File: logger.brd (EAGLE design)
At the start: 99 x 44.1 mm, 77 parts, among them IC1 LTC4412, J1 POWER_JACKPTH, Q1 FDN360P, Q2 FDN360P, Q3 2N7002PW, Q4 2N7002PW, U1 DS3231MZ/V+T, U2 FT231X-Q

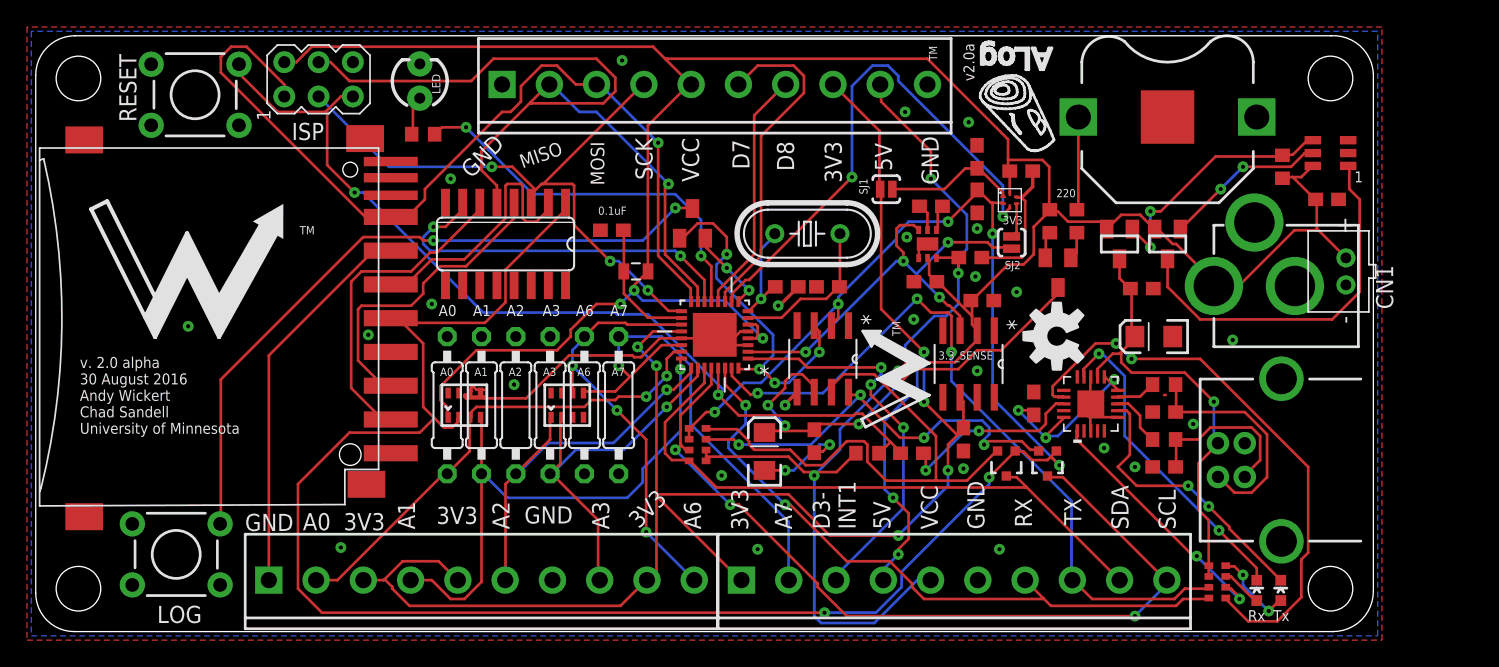
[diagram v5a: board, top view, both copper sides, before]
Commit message: Rerouted with VDD linked to RTC and SD; updated silk labels
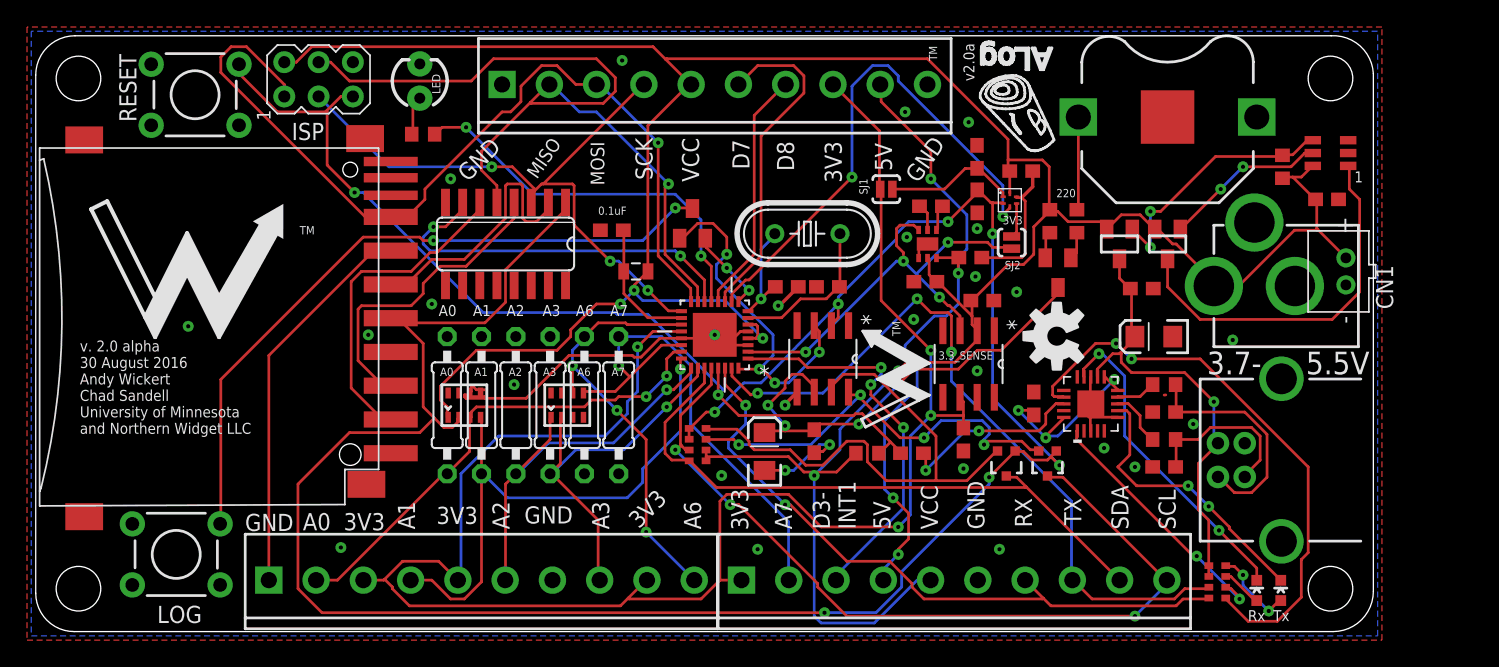
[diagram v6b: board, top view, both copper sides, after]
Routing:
- net +3V3: track 121.4 -> 131.3 mm, vias 6 -> 4
- net GND: vias 28 -> 29
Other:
- board text added: "3.7- 5.5V"
- board text added: "v. 2.0 alpha 30 August 2016 Andy Wickert Chad Sandell University of Minnesota and Northern Widget LLC"
- board text removed: "v. 2.0 alpha 30 August 2016 Andy Wickert Chad Sandell University of Minnesota"
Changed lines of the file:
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@@
 Andy Wickert
 Chad Sandell
-University of Minnesota</text>
+University of Minnesota
+and Northern Widget LLC</text>
 <text x="49.2787" y="7.5702" size="1.27" layer="21" rot="R90">A6</text>
 <text x="44.6686" y="7.5702" size="1.27" layer="21" rot="R45">3V3</text>
@@
 <text x="62.1481" y="36.1813" size="1.27" layer="21" rot="R270">5V</text>
 <text x="58.43" y="36.3083" size="1.27" layer="21" rot="R270">3V3</text>
-<text x="65.6025" y="36.6893" size="1.27" layer="21" rot="R270">GND</text>
+<text x="66.3645" y="36.8163" size="1.27" layer="21" rot="R235">GND</text>
 <text x="63.4365" y="22.987" size="0.6096" layer="21" rot="R270">TM</text>
 <text x="91.059" y="1.5875" size="0.8128" layer="21" rot="R180">Rx</text>
@@
 <text x="40.1076" y="18.9301" size="0.6096" layer="21">A6</text>
 <text x="42.6476" y="18.9301" size="0.6096" layer="21">A7</text>
-<text x="32.25503125" y="33.497734375" size="1.27" layer="21" rot="R45">GND</text>
-<text x="38.7802" y="36.3083" size="1.016" layer="21" rot="R199">MISO</text>
+<text x="32.00103125" y="33.243734375" size="1.27" layer="21" rot="R45">GND</text>
+<text x="38.1452" y="36.6893" size="1.016" layer="21" rot="R235">MISO</text>
 <text x="54.8965" y="36.3083" size="1.27" layer="21" rot="R270">D8</text>
 <text x="68.707" y="43.561" size="0.8128" layer="21" rot="R270">v2.0a</text>
+<text x="86.741" y="19.05" size="1.6764" layer="21">3.7-     5.5V</text>
 </plain>
 <attributes>
@@
 <contactref element="H1" pad="1"/>
 <contactref element="H0" pad="9"/>
-<wire x1="68.707" y1="17.018" x2="68.707" y2="15.074" width="0.2032" layer="1"/>
+<wire x1="68.707" y1="17.018" x2="68.707" y2="16.002" width="0.2032" layer="1"/>
+<wire x1="68.707" y1="16.002" x2="68.707" y2="15.074" width="0.2032" layer="1"/>
 <wire x1="68.453" y1="17.272" x2="68.707" y2="17.018" width="0.2032" layer="1"/>
 <wire x1="68.453" y1="17.272" x2="68.453" y2="17.3482" width="0.2032" layer="1"/>
@@
 <wire x1="31.242" y1="3.81" x2="29.845" y2="5.207" width="0.2032" layer="1"/>
 <wire x1="31.242" y1="3.81" x2="31.272" y2="3.81" width="0.2032" layer="1"/>
-<wire x1="45.72" y1="22.225" x2="47.8282" y2="22.225" width="0.2032" layer="1"/>
-<wire x1="44.577" y1="21.082" x2="45.72" y2="22.225" width="0.2032" layer="1"/>
-<wire x1="45.974" y1="19.685" x2="44.577" y2="21.082" width="0.2032" layer="16"/>
-<wire x1="45.974" y1="4.445" x2="45.974" y2="10.033" width="0.2032" layer="1"/>
-<wire x1="45.974" y1="10.033" x2="45.974" y2="10.16" width="0.2032" layer="1"/>
-<wire x1="45.974" y1="10.16" x2="45.974" y2="19.685" width="0.2032" layer="1"/>
-<wire x1="45.339" y1="3.81" x2="45.974" y2="4.445" width="0.2032" layer="1"/>
-<wire x1="45.339" y1="3.81" x2="45.272" y2="3.81" width="0.2032" layer="1"/>
-<wire x1="45.974" y1="10.033" x2="52.197" y2="3.81" width="0.2032" layer="1"/>
-<wire x1="52.197" y1="3.81" x2="52.272" y2="3.81" width="0.2032" layer="1"/>
 <wire x1="26.416" y1="3.302" x2="25.8445" y2="3.8735" width="0.2032" layer="1"/>
 <wire x1="26.416" y1="3.175" x2="26.416" y2="3.302" width="0.2032" layer="1"/>
 <wire x1="27.686" y1="1.905" x2="26.416" y2="3.175" width="0.2032" layer="1"/>
 <wire x1="43.307" y1="1.905" x2="27.686" y2="1.905" width="0.2032" layer="1"/>
-<wire x1="45.212" y1="3.81" x2="43.307" y2="1.905" width="0.2032" layer="1"/>
+<wire x1="45.212" y1="3.81" x2="43.8785" y2="2.4765" width="0.2032" layer="1"/>
+<wire x1="43.8785" y1="2.4765" x2="43.307" y2="1.905" width="0.2032" layer="1"/>
 <wire x1="45.212" y1="3.81" x2="45.272" y2="3.81" width="0.2032" layer="1"/>
-<wire x1="67.564" y1="13.843" x2="68.2625" y2="14.5415" width="0.2032" layer="1"/>
-<wire x1="68.2625" y1="14.5415" x2="68.707" y2="14.986" width="0.2032" layer="1"/>
-<wire x1="67.564" y1="11.938" x2="67.564" y2="13.843" width="0.2032" layer="1"/>
-<wire x1="67.564" y1="10.795" x2="67.564" y2="11.938" width="0.2032" layer="16"/>
-<wire x1="63.881" y1="7.112" x2="67.564" y2="10.795" width="0.2032" layer="16"/>
-<wire x1="58.801" y1="7.112" x2="63.881" y2="7.112" width="0.2032" layer="1"/>
-<wire x1="55.753" y1="10.16" x2="58.801" y2="7.112" width="0.2032" layer="1"/>
-<wire x1="45.974" y1="10.16" x2="55.753" y2="10.16" width="0.2032" layer="1"/>
-<wire x1="68.707" y1="14.986" x2="68.707" y2="15.074" width="0.2032" layer="1"/>
-<via x="44.577" y="21.082" extent="1-16" drill="0.3048"/>
-<via x="45.974" y="19.685" extent="1-16" drill="0.3048"/>
-<via x="67.564" y="11.938" extent="1-16" drill="0.3048"/>
-<via x="63.881" y="7.112" extent="1-16" drill="0.3048"/>
 <wire x1="62.484" y1="37.084" x2="62.484" y2="32.766" width="0.2032" layer="1"/>
 <wire x1="59.055" y1="40.513" x2="62.484" y2="37.084" width="0.2032" layer="1"/>
 <wire x1="62.484" y1="32.766" x2="62.544" y2="32.757" width="0.2032" layer="1"/>
 <wire x1="59.055" y1="40.513" x2="59.044" y2="40.513" width="0.2032" layer="1"/>
-<wire x1="62.611" y1="23.876" x2="62.611" y2="32.639" width="0.2032" layer="1"/>
-<wire x1="65.786" y1="20.701" x2="62.611" y2="23.876" width="0.2032" layer="1"/>
-<wire x1="65.786" y1="17.018" x2="65.786" y2="20.701" width="0.2032" layer="16"/>
-<wire x1="68.2625" y1="14.5415" x2="65.786" y2="17.018" width="0.2032" layer="1"/>
+<wire x1="66.294" y1="16.002" x2="68.707" y2="16.002" width="0.2032" layer="1"/>
+<wire x1="66.294" y1="20.828" x2="66.294" y2="16.002" width="0.2032" layer="16"/>
+<wire x1="62.611" y1="24.511" x2="66.294" y2="20.828" width="0.2032" layer="1"/>
+<wire x1="62.611" y1="32.639" x2="62.611" y2="24.511" width="0.2032" layer="1"/>
 <wire x1="62.611" y1="32.639" x2="62.544" y2="32.757" width="0.2032" layer="1"/>
-<via x="65.786" y="20.701" extent="1-16" drill="0.3048"/>
-<via x="65.786" y="17.018" extent="1-16" drill="0.3048"/>
+<wire x1="45.72" y1="22.225" x2="47.8282" y2="22.225" width="0.2032" layer="1"/>
+<wire x1="44.577" y1="21.082" x2="45.72" y2="22.225" width="0.2032" layer="1"/>
+<wire x1="44.577" y1="17.78" x2="44.577" y2="21.082" width="0.2032" layer="16"/>
+<wire x1="43.815" y1="17.018" x2="44.577" y2="17.78" width="0.2032" layer="16"/>
+<wire x1="43.815" y1="16.129" x2="43.815" y2="17.018" width="0.2032" layer="16"/>
+<wire x1="42.164" y1="14.478" x2="43.815" y2="16.129" width="0.2032" layer="16"/>
+<wire x1="34.29" y1="14.478" x2="42.164" y2="14.478" width="0.2032" layer="16"/>
+<wire x1="31.496" y1="11.684" x2="34.29" y2="14.478" width="0.2032" layer="16"/>
+<wire x1="31.496" y1="3.937" x2="31.496" y2="11.684" width="0.2032" layer="16"/>
+<wire x1="31.369" y1="3.81" x2="31.496" y2="3.937" width="0.2032" layer="16"/>
+<wire x1="31.369" y1="3.81" x2="31.272" y2="3.81" width="0.2032" layer="16"/>
+<wire x1="50.673" y1="3.81" x2="52.272" y2="3.81" width="0.2032" layer="1"/>
+<wire x1="49.276" y1="2.413" x2="50.673" y2="3.81" width="0.2032" layer="1"/>
+<wire x1="43.942" y1="2.413" x2="49.276" y2="2.413" width="0.2032" layer="1"/>
+<wire x1="43.942" y1="2.413" x2="43.8785" y2="2.4765" width="0.2032" layer="1"/>
+<wire x1="64.77" y1="14.478" x2="66.294" y2="16.002" width="0.2032" layer="16"/>
+<wire x1="64.77" y1="8.636" x2="64.77" y2="14.478" width="0.2032" layer="16"/>
+<wire x1="63.881" y1="7.747" x2="64.77" y2="8.636" width="0.2032" layer="16"/>
+<wire x1="58.166" y1="7.747" x2="63.881" y2="7.747" width="0.2032" layer="1"/>
+<wire x1="55.753" y1="10.16" x2="58.166" y2="7.747" width="0.2032" layer="1"/>
+<wire x1="51.181" y1="10.16" x2="55.753" y2="10.16" width="0.2032" layer="1"/>
+<wire x1="50.673" y1="9.652" x2="51.181" y2="10.16" width="0.2032" layer="1"/>
+<wire x1="50.673" y1="3.81" x2="50.673" y2="9.652" width="0.2032" layer="1"/>
+<via x="66.294" y="16.002" extent="1-16" drill="0.3048"/>
+<via x="66.294" y="20.828" extent="1-16" drill="0.3048"/>
+<via x="44.577" y="21.082" extent="1-16" drill="0.3048"/>
+<via x="63.881" y="7.747" extent="1-16" drill="0.3048"/>
 </signal>
 <signal name="SCL">
@@
 <wire x1="43.18" y1="19.685" x2="43.18" y2="21.844" width="0.2032" layer="16"/>
 <wire x1="44.0055" y1="18.8595" x2="43.18" y2="19.685" width="0.2032" layer="1"/>
+<via x="43.18" y="19.685" extent="1-16" drill="0.3048"/>
 <wire x1="55.753" y1="8.128" x2="55.753" y2="3.81" width="0.2032" layer="16"/>
 <wire x1="48.514" y1="15.367" x2="55.753" y2="8.128" width="0.2032" layer="16"/>
@@
 <wire x1="43.18" y1="21.844" x2="46.355" y2="21.844" width="0.2032" layer="16"/>
 <wire x1="55.753" y1="3.81" x2="55.772" y2="3.81" width="0.2032" layer="16"/>
-<via x="43.18" y="19.685" extent="1-16" drill="0.3048"/>
 </signal>
 <signal name="A1">
@@
 <via x="11.303" y="22.606" extent="1-16" drill="0.3048" shape="octagon"/>
 <via x="69.723" y="29.845" extent="1-16" drill="0.3048" shape="octagon"/>
+<via x="50.292" y="21.971" extent="1-16" drill="0.3048" shape="octagon"/>
+<wire x1="39.77" y1="15.864" x2="38.97" y2="17.664" width="0" layer="19" extent="1-1"/>
 </signal>
 <signal name="5V">

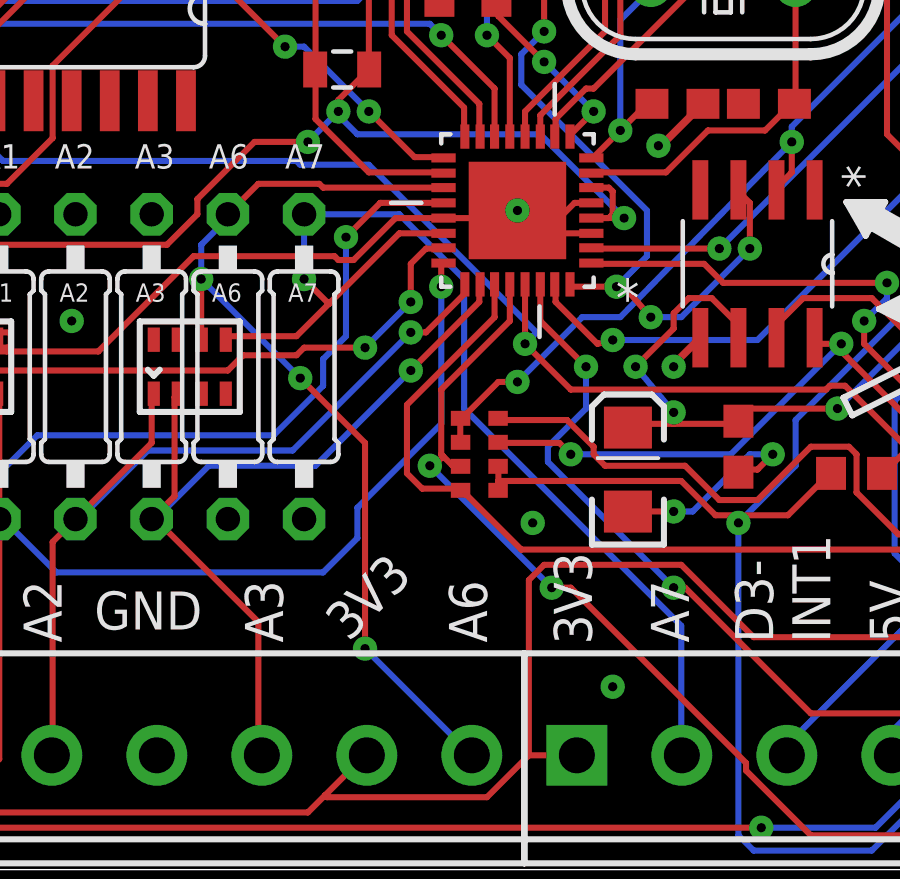
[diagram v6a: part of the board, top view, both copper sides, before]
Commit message: removed via under ground pad and fixed 1 airwire
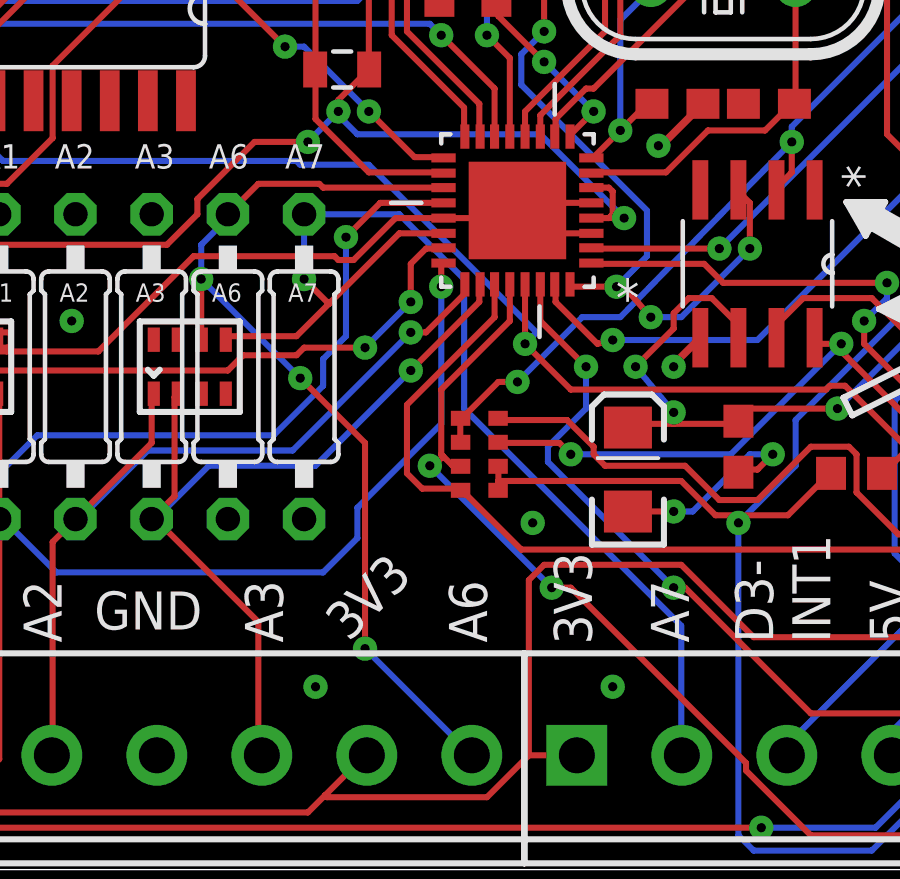
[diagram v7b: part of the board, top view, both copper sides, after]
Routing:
- net GND: track 92.1 -> 90.1 mm
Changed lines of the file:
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@@
 <param name="AutoGrid" value="0"/>
 <param name="Efforts" value="2"/>
-<param name="TopRouterVariant" value="1"/>
+<param name="TopRouterVariant" value="0"/>
 <param name="tpViaShape" value="round"/>
 <param name="PrefDir.1" value="*"/>
@@
 <wire x1="72.644" y1="32.131" x2="72.643" y2="32.194" width="0.2032" layer="1"/>
 <wire x1="70.104" y1="27.686" x2="70.065" y2="27.697" width="0.2032" layer="1"/>
-<wire x1="51.054" y1="21.209" x2="51.181" y2="21.209" width="0.2032" layer="1"/>
-<wire x1="51.181" y1="21.209" x2="52.7558" y2="21.209" width="0.2032" layer="1"/>
-<wire x1="50.292" y1="21.971" x2="51.054" y2="21.209" width="0.2032" layer="1"/>
-<wire x1="50.419" y1="21.717" x2="47.8282" y2="21.717" width="0.2032" layer="1"/>
-<wire x1="50.419" y1="21.717" x2="50.292" y2="21.971" width="0.2032" layer="1"/>
-<wire x1="52.197" y1="22.225" x2="52.7558" y2="22.225" width="0.2032" layer="1"/>
-<wire x1="51.181" y1="21.209" x2="52.197" y2="22.225" width="0.2032" layer="1"/>
-<wire x1="51.181" y1="21.209" x2="50.292" y2="21.971" width="0.2032" layer="1"/>
 <wire x1="32.258" y1="18.161" x2="32.258" y2="17.78" width="0.2032" layer="1"/>
 <wire x1="32.385" y1="18.161" x2="32.258" y2="18.161" width="0.2032" layer="1"/>
@@
 <via x="69.088" y="37.719" extent="1-16" drill="0.3048" shape="octagon"/>
 <via x="64.389" y="38.481" extent="1-16" drill="0.3048" shape="octagon"/>
-<wire x1="49.657" y1="22.86" x2="50.292" y2="22.225" width="0.254" layer="1"/>
-<wire x1="50.292" y1="22.225" x2="50.292" y2="21.971" width="0.254" layer="1"/>
 <via x="54.991" y="24.13" extent="1-16" drill="0.3048" shape="octagon"/>
 <wire x1="56.476" y1="25.527" x2="55.079" y2="24.13" width="0.254" layer="1"/>
@@
 <via x="11.303" y="22.606" extent="1-16" drill="0.3048" shape="octagon"/>
 <via x="69.723" y="29.845" extent="1-16" drill="0.3048" shape="octagon"/>
-<via x="50.292" y="21.971" extent="1-16" drill="0.3048" shape="octagon"/>
-<wire x1="39.77" y1="15.864" x2="38.97" y2="17.664" width="0" layer="19" extent="1-1"/>
+<wire x1="50.292" y1="21.971" x2="50.546" y2="22.225" width="0.2032" layer="1"/>
+<wire x1="50.546" y1="22.225" x2="52.7558" y2="22.225" width="0.2032" layer="1"/>
+<wire x1="50.292" y1="21.971" x2="51.054" y2="21.209" width="0.2032" layer="1"/>
+<wire x1="51.054" y1="21.209" x2="52.7558" y2="21.209" width="0.2032" layer="1"/>
+<wire x1="50.292" y1="21.971" x2="50.038" y2="21.717" width="0.2032" layer="1"/>
+<wire x1="50.038" y1="21.717" x2="47.8282" y2="21.717" width="0.2032" layer="1"/>
+<via x="43.561" y="6.096" extent="1-16" drill="0.3048" shape="octagon"/>
+<wire x1="52.832" y1="22.225" x2="52.7558" y2="22.225" width="0.2032" layer="1"/>
 </signal>
 <signal name="5V">
